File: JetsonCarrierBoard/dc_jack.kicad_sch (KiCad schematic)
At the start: 9 parts, among them J7 Barrel_Jack_MountingPin, Q10 AON6411

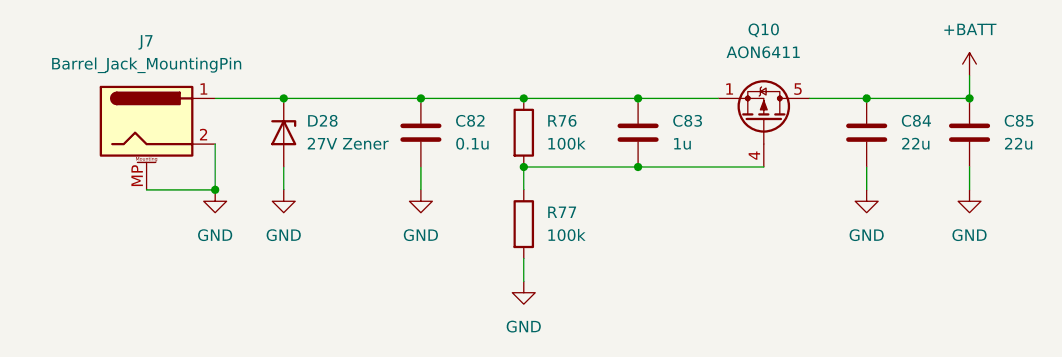
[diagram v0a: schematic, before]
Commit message: Organize and Fix USB-C Part
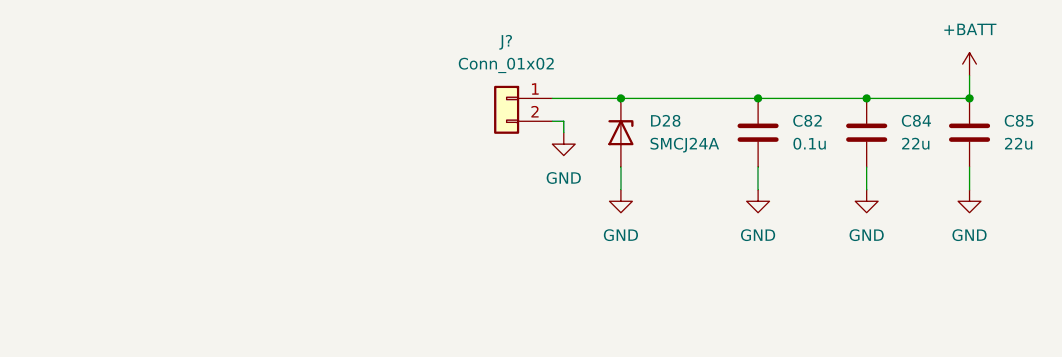
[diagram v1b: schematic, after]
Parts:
- removed C83: 1u, symbol Device:C
- removed J7: Barrel_Jack_MountingPin, symbol Connector:Barrel_Jack_MountingPin
- removed Q10: AON6411, Package_DFN_QFN:AO_DFN-8-1EP_5.55x5.2mm_P1.27mm_EP4.12x4.6mm, symbol Transistor_FET:AON6411
- removed R76, R77: 100k, symbol Device:R
- added J?: Conn_01x02, symbol Connector_Generic:Conn_01x02
- D28: value 27V Zener -> SMCJ24A
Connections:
- net +BATT: now also C82.1, D28.1 (K), J?.1 (Pin_1)
- net GND: now also J?.2 (Pin_2)
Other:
- moved on the sheet: C82, D28
